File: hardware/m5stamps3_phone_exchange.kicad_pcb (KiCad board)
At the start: 2 copper layers, 80 x 60 mm, 9 parts, among them J1 VIN 12-24V, J2 PHONE A, J3 PHONE B, J4 RING / AUDIO, U1 M5StampS3 / S007

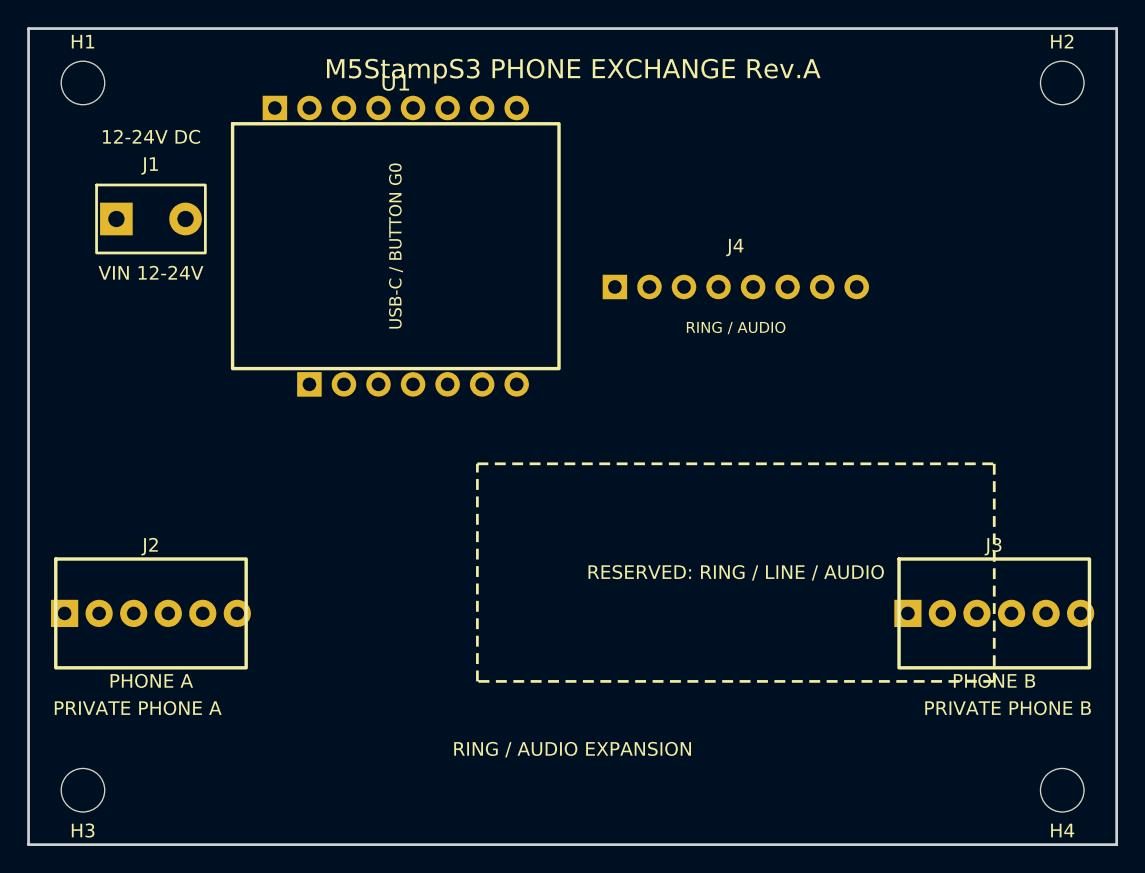
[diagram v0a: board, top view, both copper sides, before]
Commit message: 公式2.54mm DIP資料に基づきStampS3パッドを修正・未配線の製造禁止表示
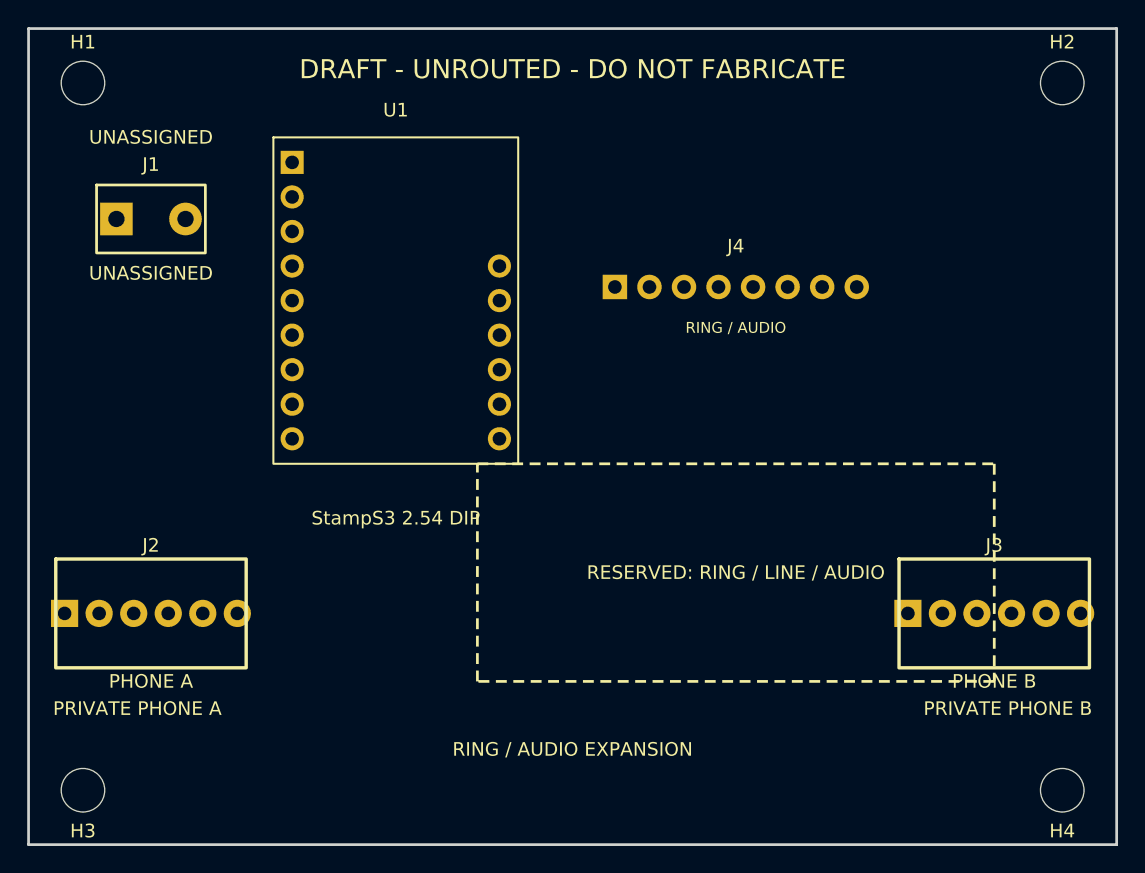
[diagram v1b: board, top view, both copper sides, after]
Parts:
- J1: value VIN 12-24V -> UNASSIGNED
- U1: value M5StampS3 / S007 -> StampS3 2.54 DIP; footprint StampS3_Carrier_Header -> StampS3_PIN2.54_DRAFT
- moved U1 4.00 mm to (47.0, 40.0)
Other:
- board text added: "DRAFT - UNROUTED - DO NOT FABRICATE"
- board text added: "UNASSIGNED"
- board text removed: "12-24V DC"
- board text removed: "M5StampS3 PHONE EXCHANGE Rev.A"
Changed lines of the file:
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@@
   (setup (pad_to_mask_clearance 0))
   (gr_rect (start 20 20) (end 100 80) (stroke (width 0.2) (type default)) (fill none) (layer "Edge.Cuts"))
-  (gr_text "M5StampS3 PHONE EXCHANGE Rev.A" (at 60 23) (layer "F.SilkS") (effects (font (size 1.4 1.4) (thickness 0.25))))
+  (gr_text "DRAFT - UNROUTED - DO NOT FABRICATE" (at 60 23) (layer "F.SilkS") (effects (font (size 1.4 1.4) (thickness 0.25))))
   (gr_text "PRIVATE PHONE A" (at 28 70) (layer "F.SilkS") (effects (font (size 1 1) (thickness 0.18))))
   (gr_text "PRIVATE PHONE B" (at 92 70) (layer "F.SilkS") (effects (font (size 1 1) (thickness 0.18))))
-  (gr_text "12-24V DC" (at 29 28) (layer "F.SilkS") (effects (font (size 1 1) (thickness 0.18))))
+  (gr_text "UNASSIGNED" (at 29 28) (layer "F.SilkS") (effects (font (size 1 1) (thickness 0.18))))
   (gr_text "RING / AUDIO EXPANSION" (at 60 73) (layer "F.SilkS") (effects (font (size 1 1) (thickness 0.18))))
   (footprint "MountingHole_3.2mm" (layer "F.Cu") (at 24 24)
@@
     (property "Reference" "H4" (at 0 3 0) (layer "F.SilkS") (effects (font (size 1 1) (thickness 0.15))))
     (pad "" np_thru_hole circle (at 0 0) (size 3.2 3.2) (drill 3.2) (layers "*.Cu" "*.Mask")))
-  (footprint "StampS3_Carrier_Header" (layer "F.Cu") (at 47 36)
-    (property "Reference" "U1" (at 0 -12 0) (layer "F.SilkS") (effects (font (size 1.2 1.2) (thickness 0.2))))
-    (property "Value" "M5StampS3 / S007" (at 0 12 0) (layer "F.Fab") hide (effects (font (size 1 1) (thickness 0.15))))
-    (fp_rect (start -12 -9) (end 12 9) (stroke (width 0.25) (type default)) (fill none) (layer "F.SilkS"))
-    (fp_text user "USB-C / BUTTON G0" (at 0 0 90) (layer "F.SilkS") (effects (font (size 0.9 0.9) (thickness 0.15))))
-    (pad "1" thru_hole rect (at -8.89 -10.16) (size 1.8 1.8) (drill 1) (layers "*.Cu" "*.Mask"))
-    (pad "2" thru_hole circle (at -6.35 -10.16) (size 1.8 1.8) (drill 1) (layers "*.Cu" "*.Mask"))
-    (pad "3" thru_hole circle (at -3.81 -10.16) (size 1.8 1.8) (drill 1) (layers "*.Cu" "*.Mask"))
-    (pad "4" thru_hole circle (at -1.27 -10.16) (size 1.8 1.8) (drill 1) (layers "*.Cu" "*.Mask"))
-    (pad "5" thru_hole circle (at 1.27 -10.16) (size 1.8 1.8) (drill 1) (layers "*.Cu" "*.Mask"))
-    (pad "6" thru_hole circle (at 3.81 -10.16) (size 1.8 1.8) (drill 1) (layers "*.Cu" "*.Mask"))
-    (pad "7" thru_hole circle (at 6.35 -10.16) (size 1.8 1.8) (drill 1) (layers "*.Cu" "*.Mask"))
-    (pad "8" thru_hole circle (at 8.89 -10.16) (size 1.8 1.8) (drill 1) (layers "*.Cu" "*.Mask"))
-    (pad "9" thru_hole rect (at -6.35 10.16) (size 1.8 1.8) (drill 1) (layers "*.Cu" "*.Mask"))
-    (pad "10" thru_hole circle (at -3.81 10.16) (size 1.8 1.8) (drill 1) (layers "*.Cu" "*.Mask"))
-    (pad "11" thru_hole circle (at -1.27 10.16) (size 1.8 1.8) (drill 1) (layers "*.Cu" "*.Mask"))
-    (pad "12" thru_hole circle (at 1.27 10.16) (size 1.8 1.8) (drill 1) (layers "*.Cu" "*.Mask"))
-    (pad "13" thru_hole circle (at 3.81 10.16) (size 1.8 1.8) (drill 1) (layers "*.Cu" "*.Mask"))
-    (pad "14" thru_hole circle (at 6.35 10.16) (size 1.8 1.8) (drill 1) (layers "*.Cu" "*.Mask"))
-    (pad "15" thru_hole circle (at 8.89 10.16) (size 1.8 1.8) (drill 1) (layers "*.Cu" "*.Mask")))
+  (footprint "StampS3_PIN2.54_DRAFT" (layer "F.Cu") (at 47 40)
+    (fp_text reference "U1" (at 0 -14) (layer "F.SilkS") (effects (font (size 1 1) (thickness 0.15))))
+    (fp_text value "StampS3 2.54 DIP" (at 0 16) (layer "F.SilkS") (effects (font (size 1 1) (thickness 0.15))))
+    (fp_rect (start -9 -12) (end 9 12) (stroke (width 0.15) (type default)) (fill none) (layer "F.SilkS"))
+    (pad "1" thru_hole rect (at -7.62 -10.160003) (size 1.7 1.7) (drill 1) (layers "*.Cu" "*.Mask"))
+    (pad "3" thru_hole circle (at -7.62 -7.619998) (size 1.7 1.7) (drill 1) (layers "*.Cu" "*.Mask"))
+    (pad "5" thru_hole circle (at -7.62 -5.08) (size 1.7 1.7) (drill 1) (layers "*.Cu" "*.Mask"))
+    (pad "7" thru_hole circle (at -7.62 -2.54) (size 1.7 1.7) (drill 1) (layers "*.Cu" "*.Mask"))
+    (pad "9" thru_hole circle (at -7.62 0.000002) (size 1.7 1.7) (drill 1) (layers "*.Cu" "*.Mask"))
+    (pad "11" thru_hole circle (at -7.62 2.54) (size 1.7 1.7) (drill 1) (layers "*.Cu" "*.Mask"))
+    (pad "13" thru_hole circle (at -7.62 5.08) (size 1.7 1.7) (drill 1) (layers "*.Cu" "*.Mask"))
+    (pad "15" thru_hole circle (at -7.62 7.62) (size 1.7 1.7) (drill 1) (layers "*.Cu" "*.Mask"))
+    (pad "17" thru_hole circle (at -7.62 10.16) (size 1.7 1.7) (drill 1) (layers "*.Cu" "*.Mask"))
+    (pad "18" thru_hole circle (at 7.62 10.160004 180) (size 1.7 1.7) (drill 1) (layers "*.Cu" "*.Mask"))
+    (pad "20" thru_hole circle (at 7.62 7.620004 180) (size 1.7 1.7) (drill 1) (layers "*.Cu" "*.Mask"))
+    (pad "22" thru_hole circle (at 7.62 5.080007 180) (size 1.7 1.7) (drill 1) (layers "*.Cu" "*.Mask"))
+    (pad "24" thru_hole circle (at 7.62 2.540004 180) (size 1.7 1.7) (drill 1) (layers "*.Cu" "*.Mask"))
+    (pad "26" thru_hole circle (at 7.62 0.000004 180) (size 1.7 1.7) (drill 1) (layers "*.Cu" "*.Mask"))
+    (pad "28" thru_hole circle (at 7.62 -2.539996 180) (size 1.7 1.7) (drill 1) (layers "*.Cu" "*.Mask"))
+  )
   (footprint "TerminalBlock_1x02_P5.08mm" (layer "F.Cu") (at 29 34)
     (property "Reference" "J1" (at 0 -4 0) (layer "F.SilkS") (effects (font (size 1 1) (thickness 0.15))))
-    (property "Value" "VIN 12-24V" (at 0 4 0) (layer "F.SilkS") (effects (font (size 1 1) (thickness 0.15))))
+    (property "Value" "UNASSIGNED" (at 0 4 0) (layer "F.SilkS") (effects (font (size 1 1) (thickness 0.15))))
     (fp_rect (start -4 -2.5) (end 4 2.5) (stroke (width 0.2) (type default)) (fill none) (layer "F.SilkS"))
     (pad "1" thru_hole rect (at -2.54 0) (size 2.4 2.4) (drill 1.2) (layers "*.Cu" "*.Mask"))
